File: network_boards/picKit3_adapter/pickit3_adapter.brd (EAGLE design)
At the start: 63.5 x 38.1 mm, 2 parts, among them P1 ICSP

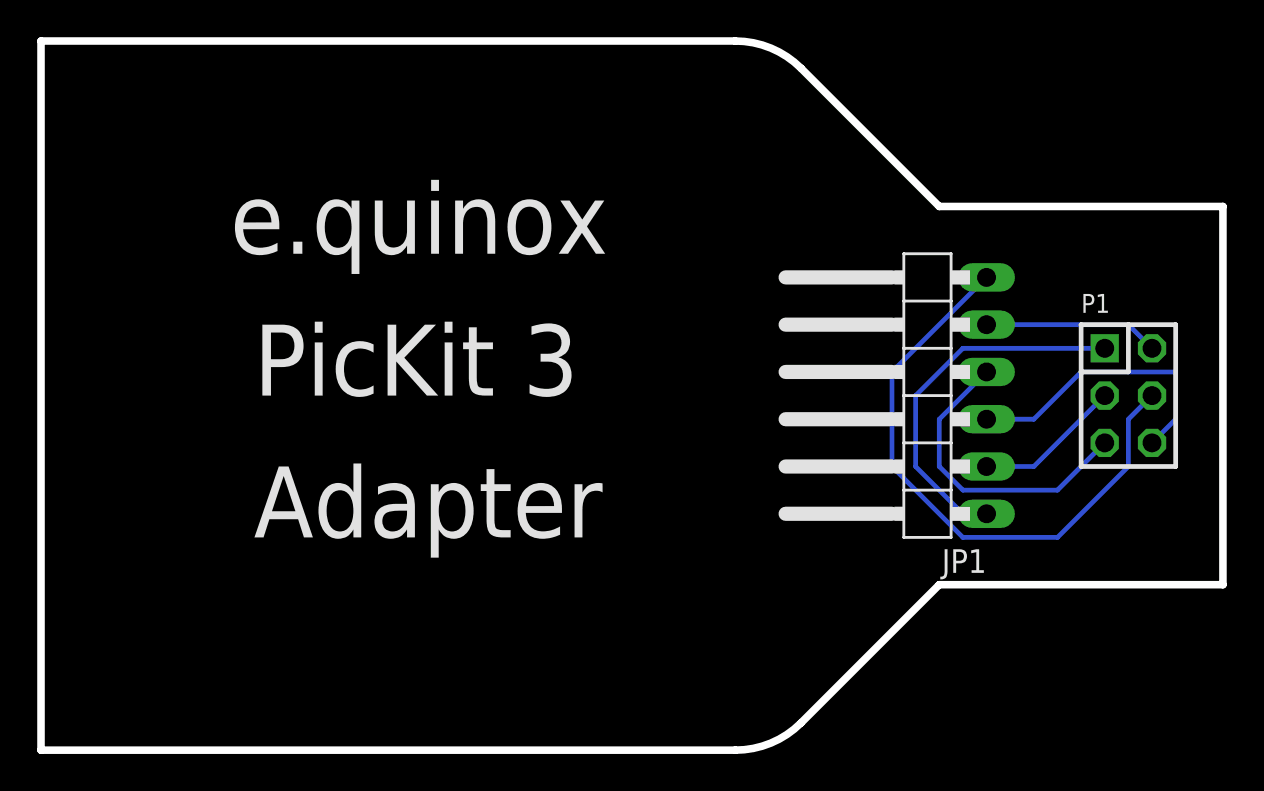
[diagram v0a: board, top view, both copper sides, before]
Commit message: Minor modifications to PicKit 3 adaptor
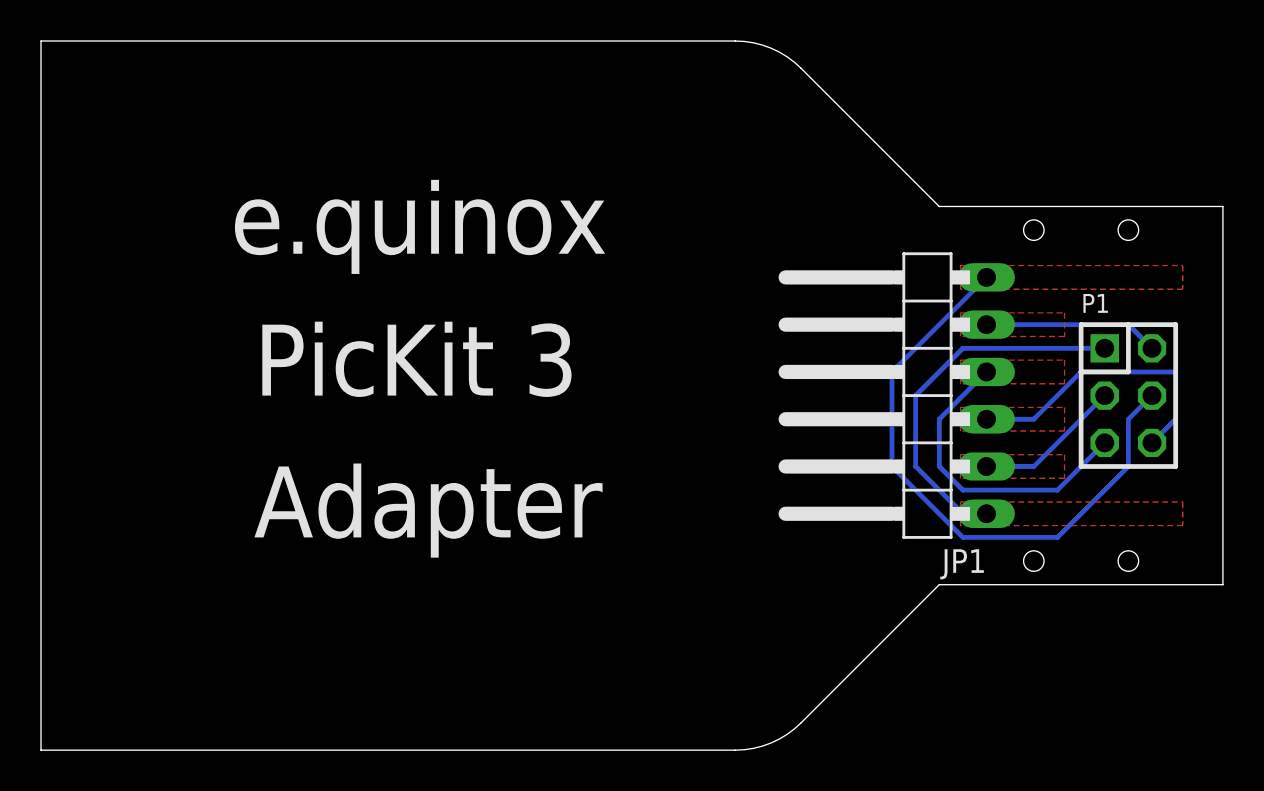
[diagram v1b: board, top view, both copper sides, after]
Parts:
- added U$1: (no value), eko-parts:EQNXLOGO
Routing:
- added copper zone on layer 1, net !MCLR!
- added copper zone on layer 1, net +3V3
- added copper zone on layer 1, net 0V
- added copper zone on layer 1, net PGC
- added copper zone on layer 1, net PGD
- added copper zone on layer 1, net PGM

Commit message: Resized pickit adaptor to fit into 5x5 pcb
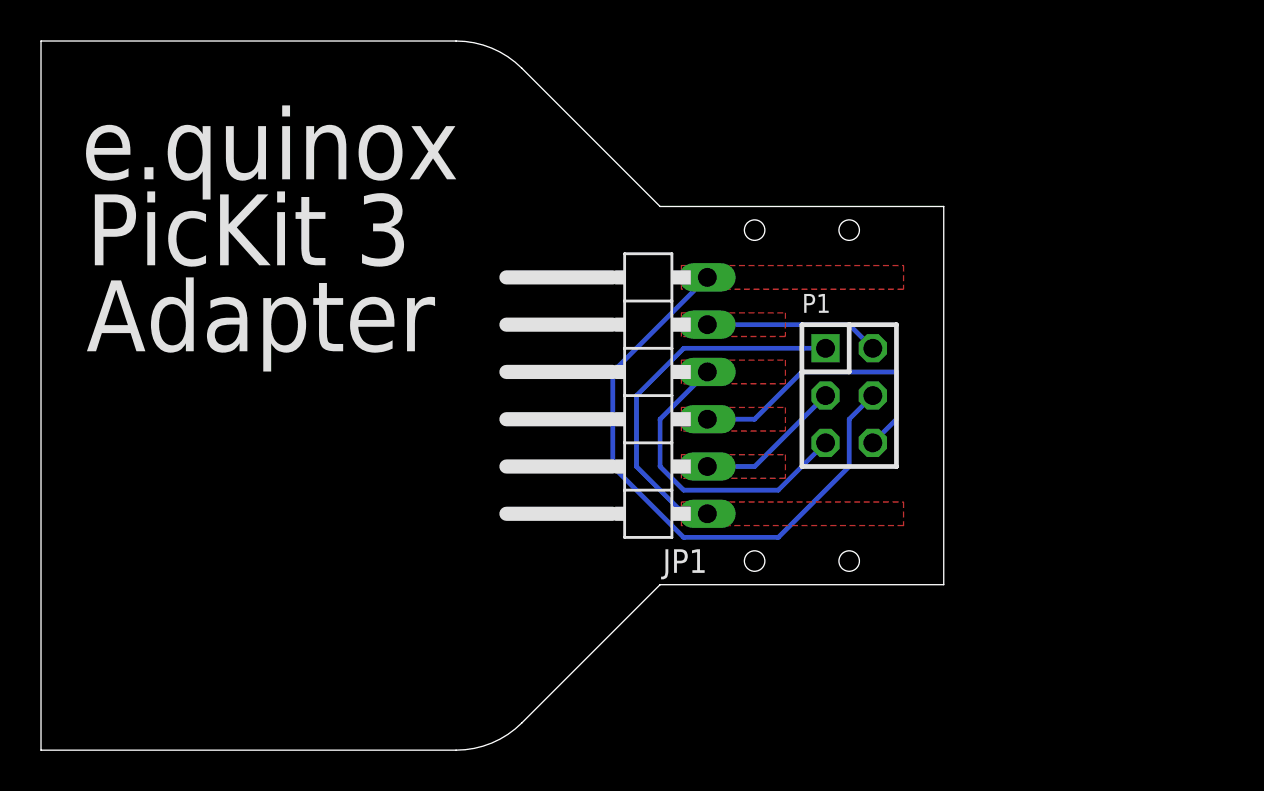
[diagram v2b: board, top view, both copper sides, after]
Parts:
- moved JP1 15.0 mm to (32.0, 19.1)
- moved P1 15.0 mm to (43.4, 19.1)
- moved U$1 13.0 mm to (9.86, 19.1)
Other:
- board size 63.5 x 38.1 mm -> 48.5 x 38.1 mm
